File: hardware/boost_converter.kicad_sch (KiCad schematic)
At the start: 11 parts, among them SW1 SW_SPDT, U5 TPS61200DRC

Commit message: Removed comments on UART, added some footprints and started fixing rule checks
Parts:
- C10, C9: Manuf. Part # (none) -> GRM21BR71H104KA01L; Part Num GRM21BR71H104KA01L -> (none); Price/unit $0.0097 -> (none); Supplier Name (none) -> JLCPCB; Supplier Unit Price (none) -> $0.0097
- SW1: Supplier Name (none) -> JLCPCB
- U5: Manuf. Part # (none) -> TPS61200DRCR; Part Num TPS61200DRCR -> (none); Price/unit $1.4430 -> (none); Supplier Name (none) -> JLCPCB; Supplier Unit Price (none) -> $1.4430
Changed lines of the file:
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@@
+			)
+		)
+		(property "Supplier Name" ""
+			(at 193.04 106.68 0)
+			(effects
+				(font
+					(size 1.27 1.27)
+				)
+				(hide yes)
 			)
 		)
@@
 			)
 		)
+		(property "Supplier Name" ""
+			(at 118.11 111.76 0)
+			(effects
+				(font
+					(size 1.27 1.27)
+				)
+				(hide yes)
+			)
+		)
 		(pin "2"
 		)
@@
 			)
 		)
+		(property "Supplier Name" ""
+			(at 148.59 87.63 0)
+			(effects
+				(font
+					(size 1.27 1.27)
+				)
+				(hide yes)
+			)
+		)
 		(pin "1"
 		)
@@
 			)
 		)
-		(property "Part Num" "GRM21BR71H104KA01L"
-			(at 170.18 110.49 0)
-			(effects
-				(font
-					(size 1.27 1.27)
-				)
-				(hide yes)
-			)
-		)
-		(property "Price/unit" "$0.0097"
-			(at 170.18 110.49 0)
-			(effects
-				(font
-					(size 1.27 1.27)
-				)
-				(hide yes)
-			)
-		)
 		(property "Supplier Link" "https://jlcpcb.com/partdetail/MurataElectronics-GRM21BR71H104KA01L/C77082"
 			(at 170.18 110.49 0)
@@
 			)
 		)
+		(property "Supplier Name" "JLCPCB"
+			(at 170.18 110.49 0)
+			(effects
+				(font
+					(size 1.27 1.27)
+				)
+				(hide yes)
+			)
+		)
+		(property "Manuf. Part #" "GRM21BR71H104KA01L"
+			(at 170.18 110.49 0)
+			(effects
+				(font
+					(size 1.27 1.27)
+				)
+				(hide yes)
+			)
+		)
+		(property "Supplier Unit Price" "$0.0097"
+			(at 170.18 110.49 0)
+			(effects
+				(font
+					(size 1.27 1.27)
+				)
+				(hide yes)
+			)
+		)
 		(pin "1"
 		)
@@
 			)
 		)
+		(property "Supplier Name" ""
+			(at 110.49 105.41 0)
+			(effects
+				(font
+					(size 1.27 1.27)
+				)
+				(hide yes)
+			)
+		)
 		(pin "1"
 		)
@@
 		)
 		(property "Description" "Resistor, small symbol"
+			(at 184.15 111.76 0)
+			(effects
+				(font
+					(size 1.27 1.27)
+				)
+				(hide yes)
+			)
+		)
+		(property "Supplier Name" ""
 			(at 184.15 111.76 0)
 			(effects
@@
 			)
 		)
-		(property "Price/unit" ""
-			(at 44.45 149.86 0)
-			(effects
-				(font
-					(size 1.27 1.27)
-				)
-				(hide yes)
-			)
-		)
-		(property "Part Num" ""
-			(at 44.45 149.86 0)
-			(effects
-				(font
-					(size 1.27 1.27)
-				)
-				(hide yes)
-			)
-		)
 		(property "Package" ""
 			(at 44.45 149.86 0)
@@
 			)
 		)
+		(property "Supplier Name" "JLCPCB"
+			(at 44.45 149.86 0)
+			(effects
+				(font
+					(size 1.27 1.27)
+				)
+				(hide yes)
+			)
+		)
 		(pin "3"
 		)
@@
 			)
 		)
+		(property "Supplier Name" ""
+			(at 184.15 101.6 0)
+			(effects
+				(font
+					(size 1.27 1.27)
+				)
+				(hide yes)
+			)
+		)
 		(pin "2"
 		)
@@
 			)
 		)
-		(property "Part Num" "GRM21BR71H104KA01L"
-			(at 124.46 100.33 0)
-			(effects
-				(font
-					(size 1.27 1.27)
-				)
-				(hide yes)
-			)
-		)
-		(property "Price/unit" "$0.0097"
-			(at 124.46 100.33 0)
-			(effects
-				(font
-					(size 1.27 1.27)
-				)
-				(hide yes)
-			)
-		)
 		(property "Supplier Link" "https://jlcpcb.com/partdetail/MurataElectronics-GRM21BR71H104KA01L/C77082"
 			(at 124.46 100.33 0)
@@
 			)
 		)
+		(property "Supplier Name" "JLCPCB"
+			(at 124.46 100.33 0)
+			(effects
+				(font
+					(size 1.27 1.27)
+				)
+				(hide yes)
+			)
+		)
+		(property "Manuf. Part #" "GRM21BR71H104KA01L"
+			(at 124.46 100.33 0)
+			(effects
+				(font
+					(size 1.27 1.27)
+				)
+				(hide yes)
+			)
+		)
+		(property "Supplier Unit Price" "$0.0097"
+			(at 124.46 100.33 0)
+			(effects
+				(font
+					(size 1.27 1.27)
+				)
+				(hide yes)
+			)
+		)
 		(pin "1"
 		)
@@
 			)
 		)
+		(property "Supplier Name" ""
+			(at 118.11 100.33 0)
+			(effects
+				(font
+					(size 1.27 1.27)
+				)
+				(hide yes)
+			)
+		)
 		(pin "2"
 		)
@@
 			)
 		)
-		(property "Price/unit" "$1.4430"
-			(at 148.59 100.33 0)
-			(effects
-				(font
-					(size 1.27 1.27)
-				)
-				(hide yes)
-			)
-		)
-		(property "Part Num" "TPS61200DRCR"
-			(at 148.59 100.33 0)
-			(effects
-				(font
-					(size 1.27 1.27)
-				)
-				(hide yes)
-			)
-		)
 		(property "Package" "VSON-10-EP(3x3)"
 			(at 148.59 100.33 0)
 			(effects
+				(font
+					(size 1.27 1.27)
+				)
+				(hide yes)
+			)
+		)
+		(property "Supplier Name" "JLCPCB"
+			(at 148.59 100.33 0)
+			(effects
+				(font
+					(size 1.27 1.27)
+				)
+				(hide yes)
+			)
+		)
+		(property "Manuf. Part #" "TPS61200DRCR"
+			(at 148.59 100.33 0)
+			(effects
+				(font
+					(size 1.27 1.27)
+				)
+				(hide yes)
+			)
+		)
+		(property "Supplier Unit Price" "$1.4430"
+			(at 148.59 100.33 0)
+			(effects

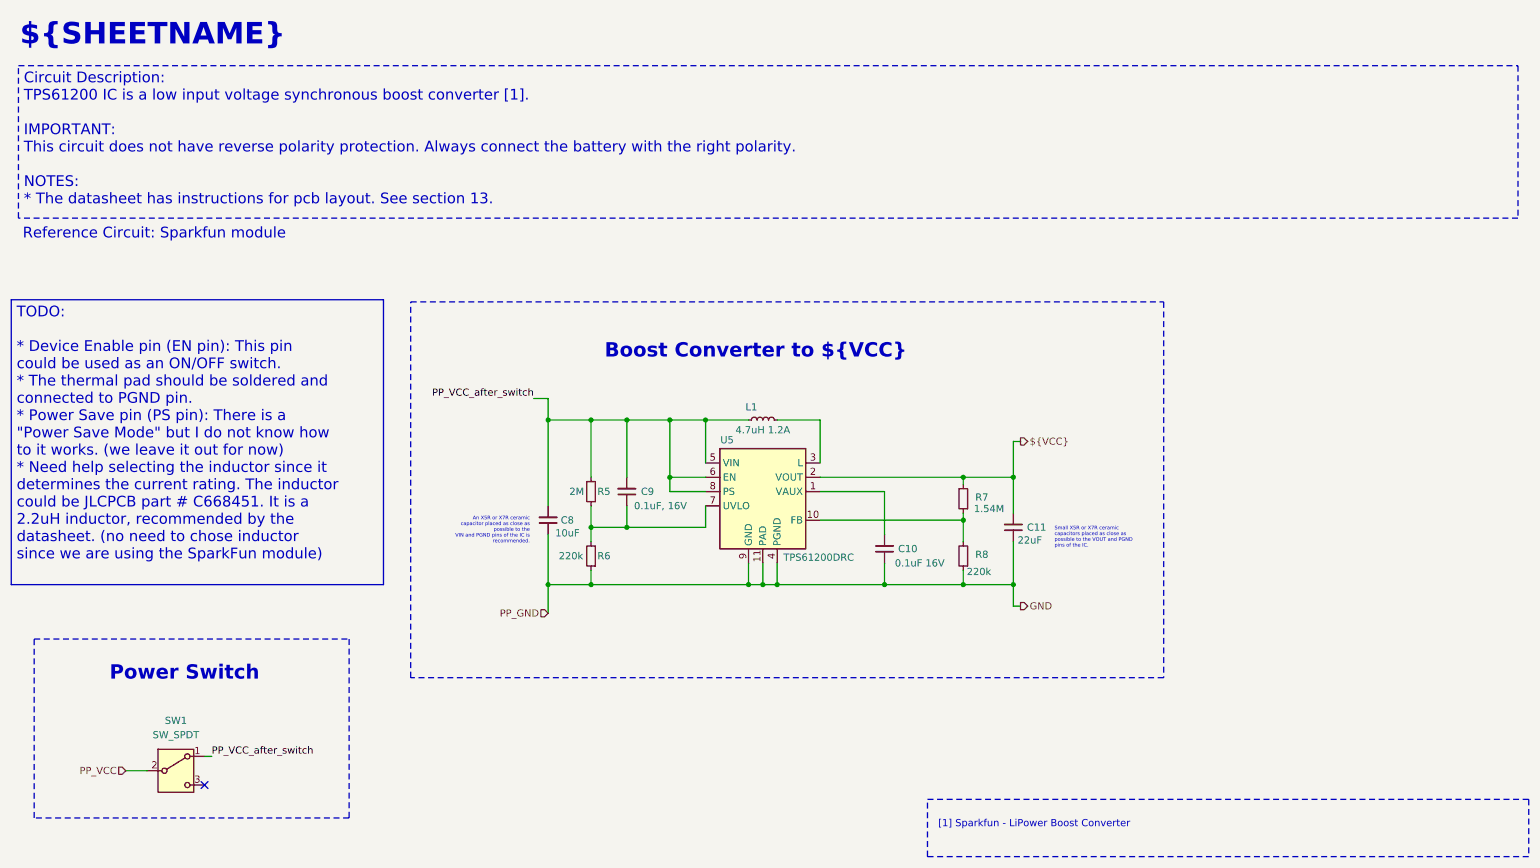
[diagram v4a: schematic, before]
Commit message: Added switch footprint, SparkFun_LiPower footprint
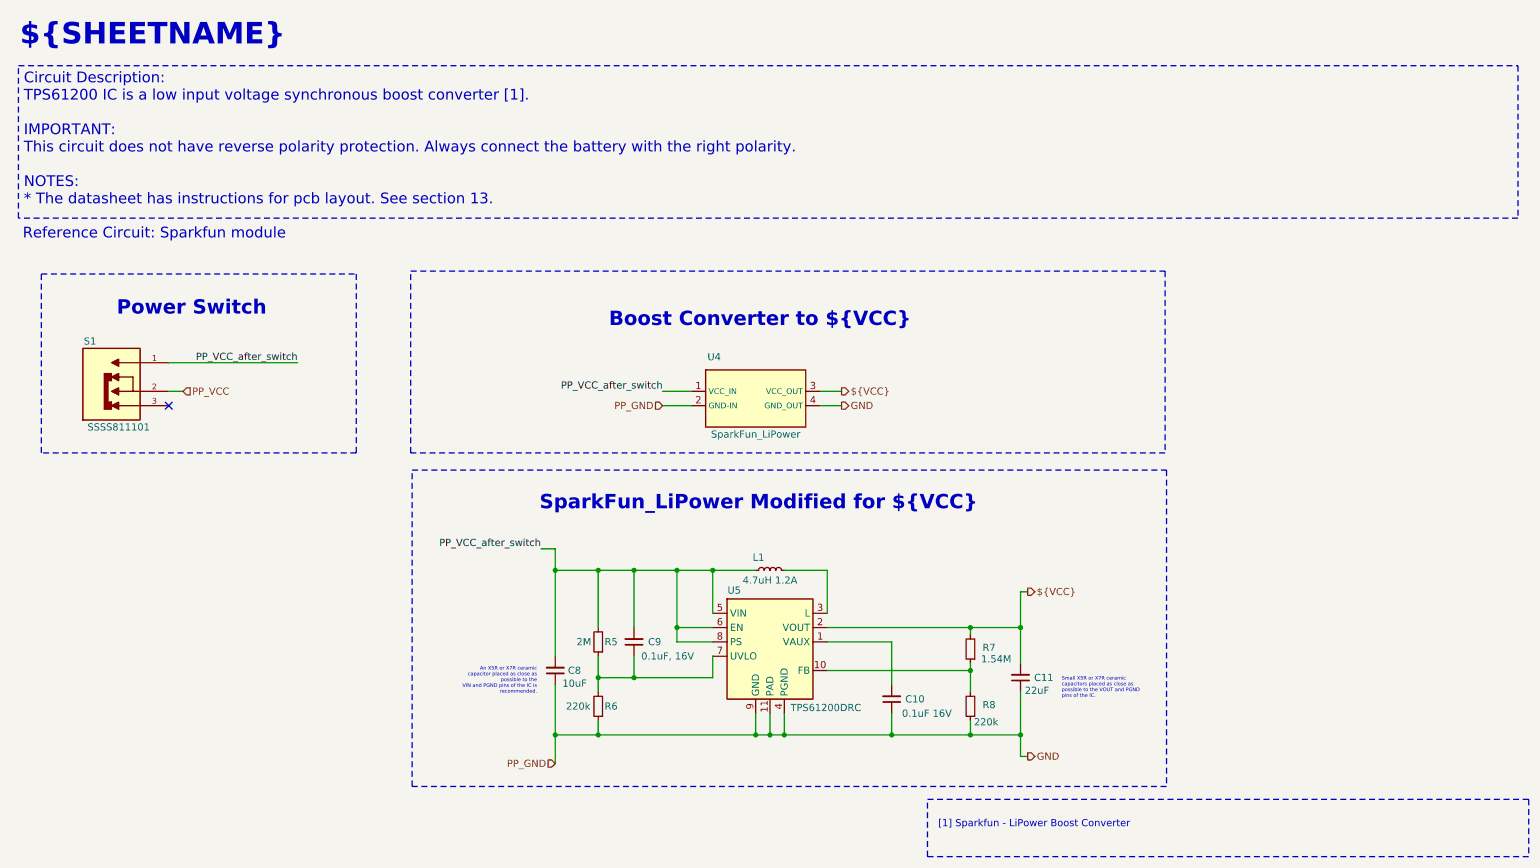
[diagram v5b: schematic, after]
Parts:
- removed SW1: SW_SPDT, symbol Switch:SW_SPDT
- added S1: SSSS811101, kitchen_timer:SW_SSSS811101, symbol kitchen_timer-symbols_lib:SSSS811101
- added U4: SparkFun_LiPower, kitchen_timer:SparkFun_LiPower, symbol kitchen_timer-symbols_lib:Sparkfun_LiPower-Boost_Converter
- C10, C11, C8, C9, L1, R5, R6, R7, R8, U5: now left out of the parts list
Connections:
- net ${VCC}: now also U4.3 (VCC_OUT)
- net GND: now also U4.2 (GND-IN), U4.4 (GND_OUT)
- net PP_VCC: now also S1.2
- net PP_VCC_after_switch: now also S1.1, U4.1 (VCC_IN)
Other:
- note added: "SparkFun_LiPower Modified for ${VCC}"
- moved on the sheet: C10, C11, C8, C9, L1, R5, R6, R7, R8, U5

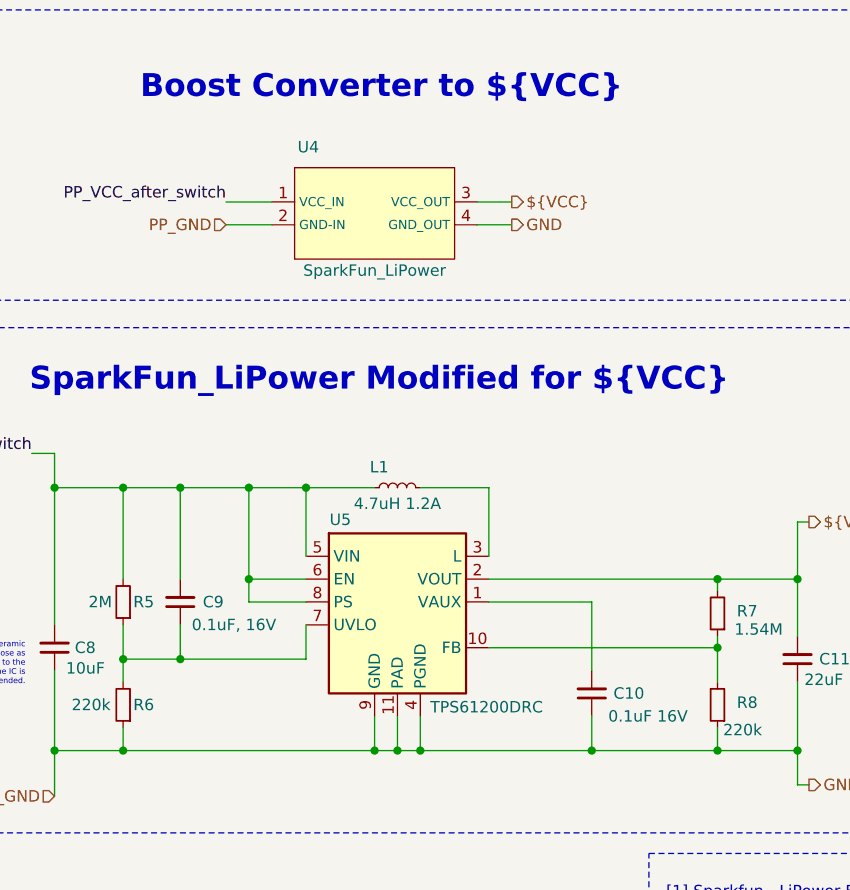
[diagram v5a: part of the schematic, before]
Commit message: Added many footprints and populated part of the property tables
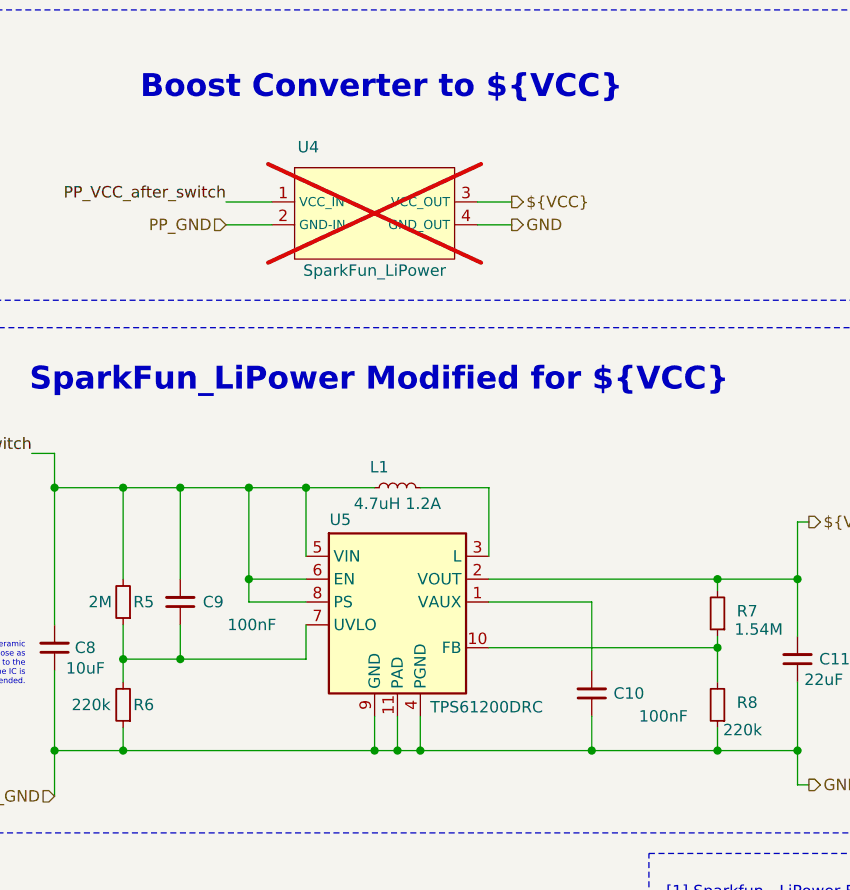
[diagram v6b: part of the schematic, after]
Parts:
- C10: value 0.1uF 16V -> 100nF; footprint (none) -> Capacitor_SMD:C_0805_2012Metric_Pad1.18x1.45mm_HandSolder; Manuf. Name (none) -> Murata Electronics; Supplier Link https://jlcpcb.com/partdetail/MurataElectronics-GRM21BR71H104KA01L/C77082 -> https://jlcpcb.com/partdetail/MurataElectronics-GRM21BR71H104KA01L/C77082; Supplier Part # (none) -> C77082; Supplier Unit Price $0.0097 -> $0.0099
- C11, C8: footprint (none) -> ~
- C9: value 0.1uF, 16V -> 100nF; footprint (none) -> Capacitor_SMD:C_0805_2012Metric_Pad1.18x1.45mm_HandSolder; Manuf. Name (none) -> Murata Electronics; Supplier Link https://jlcpcb.com/partdetail/MurataElectronics-GRM21BR71H104KA01L/C77082 -> https://jlcpcb.com/partdetail/MurataElectronics-GRM21BR71H104KA01L/C77082; Supplier Part # (none) -> C77082; Supplier Unit Price $0.0097 -> $0.0099
- U4: now not fitted; now left out of the parts list
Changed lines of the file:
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@@
 			)
 		)
-		(property "Footprint" ""
+		(property "Footprint" "~"
 			(at 194.31 133.35 0)
 			(effects
@@
 			)
 		)
-		(property "Description" "Unpolarized capacitor, small symbol"
+		(property "Description" "22uF Unpolarized capacitor"
 			(at 194.31 133.35 0)
 			(effects
@@
 			)
 		)
-		(property "Supplier Name" ""
+		(property "Supplier Name" "~"
+			(at 194.31 133.35 0)
+			(effects
+				(font
+					(size 1.27 1.27)
+				)
+				(hide yes)
+			)
+		)
+		(property "Manuf. Name" "~"
+			(at 194.31 133.35 0)
+			(effects
+				(font
+					(size 1.27 1.27)
+				)
+				(hide yes)
+			)
+		)
+		(property "Manuf. Part #" "~"
+			(at 194.31 133.35 0)
+			(effects
+				(font
+					(size 1.27 1.27)
+				)
+				(hide yes)
+			)
+		)
+		(property "Package" "~"
+			(at 194.31 133.35 0)
+			(effects
+				(font
+					(size 1.27 1.27)
+				)
+				(hide yes)
+			)
+		)
+		(property "Supplier Link" "~"
+			(at 194.31 133.35 0)
+			(effects
+				(font
+					(size 1.27 1.27)
+				)
+				(hide yes)
+			)
+		)
+		(property "Supplier Part #" "~"
+			(at 194.31 133.35 0)
+			(effects
+				(font
+					(size 1.27 1.27)
+				)
+				(hide yes)
+			)
+		)
+		(property "Supplier Unit Price" "~"
 			(at 194.31 133.35 0)
 			(effects
@@
 			)
 		)
-		(property "Supplier Name" ""
+		(property "Supplier Name" "~"
 			(at 149.86 114.3 0)
 			(effects
@@
 				)
 				(hide yes)
+			)
+		)
+		(property "Manuf. Name" "~"
+			(at 149.86 114.3 0)
+			(effects
+				(font
+					(size 1.27 1.27)
+				)
+			)
+		)
+		(property "Manuf. Part #" "~"
+			(at 149.86 114.3 0)
+			(effects
+				(font
+					(size 1.27 1.27)
+				)
+			)
+		)
+		(property "Package" "~"
+			(at 149.86 114.3 0)
+			(effects
+				(font
+					(size 1.27 1.27)
+				)
+			)
+		)
+		(property "Supplier Link" "~"
+			(at 149.86 114.3 0)
+			(effects
+				(font
+					(size 1.27 1.27)
+				)
+			)
+		)
+		(property "Supplier Part #" "~"
+			(at 149.86 114.3 0)
+			(effects
+				(font
+					(size 1.27 1.27)
+				)
+			)
+		)
+		(property "Supplier Unit Price" "~"
+			(at 149.86 114.3 0)
+			(effects
+				(font
+					(size 1.27 1.27)
+				)
 			)
 		)
@@
 			)
 		)
-		(property "Value" "0.1uF 16V"
+		(property "Value" "100nF"
 			(at 182.118 139.7 0)
 			(effects
@@
 			)
 		)
-		(property "Footprint" ""
+		(property "Footprint" "Capacitor_SMD:C_0805_2012Metric_Pad1.18x1.45mm_HandSolder"
 			(at 171.45 137.16 0)
 			(effects
@@
 			)
 		)
-		(property "Description" "Unpolarized capacitor, small symbol"
+		(property "Description" "100nF Unpolarized capacitor"
 			(at 171.45 137.16 0)
 			(effects
@@
 			)
 		)
-		(property "Supplier Link" "https://jlcpcb.com/partdetail/MurataElectronics-GRM21BR71H104KA01L/C77082"
+		(property "Supplier Link" "https://jlcpcb.com/partdetail/MurataElectronics-GRM21BR71H104KA01L/C77082 "
 			(at 171.45 137.16 0)
 			(effects
@@
 			)
 		)
-		(property "Supplier Unit Price" "$0.0097"
+		(property "Supplier Unit Price" " $0.0099"
+			(at 171.45 137.16 0)
+			(effects
+				(font
+					(size 1.27 1.27)
+				)
+				(hide yes)
+			)
+		)
+		(property "Manuf. Name" " Murata Electronics"
+			(at 171.45 137.16 0)
+			(effects
+				(font
+					(size 1.27 1.27)
+				)
+				(hide yes)
+			)
+		)
+		(property "Supplier Part #" "C77082"
 			(at 171.45 137.16 0)
 			(effects
@@
 			)
 		)
-		(property "Footprint" ""
+		(property "Footprint" "~"
 			(at 111.76 132.08 0)
 			(effects
@@
 			)
 		)
-		(property "Description" "Unpolarized capacitor, small symbol"
+		(property "Description" "10uF Unpolarized capacitor"
 			(at 111.76 132.08 0)
 			(effects
@@
 			)
 		)
-		(property "Supplier Name" ""
+		(property "Supplier Name" "~"
+			(at 111.76 132.08 0)
+			(effects
+				(font
+					(size 1.27 1.27)
+				)
+				(hide yes)
+			)
+		)
+		(property "Manuf. Name" "~"
+			(at 111.76 132.08 0)
+			(effects
+				(font
+					(size 1.27 1.27)
+				)
+				(hide yes)
+			)
+		)
+		(property "Manuf. Part #" "~"
+			(at 111.76 132.08 0)
+			(effects
+				(font
+					(size 1.27 1.27)
+				)
+				(hide yes)
+			)
+		)
+		(property "Package" "~"
+			(at 111.76 132.08 0)
+			(effects
+				(font
+					(size 1.27 1.27)
+				)
+				(hide yes)
+			)
+		)
+		(property "Supplier Link" "~"
+			(at 111.76 132.08 0)
+			(effects
+				(font
+					(size 1.27 1.27)
+				)
+				(hide yes)
+			)
+		)
+		(property "Supplier Part #" "~"
+			(at 111.76 132.08 0)
+			(effects
+				(font
+					(size 1.27 1.27)
+				)
+				(hide yes)
+			)
+		)
+		(property "Supplier Unit Price" "~"
 			(at 111.76 132.08 0)
 			(effects
@@
 			)
 		)
-		(property "Value" "0.1uF, 16V"
+		(property "Value" "100nF"
 			(at 136.398 129.54 0)
 			(effects
@@
 			)
 		)
-		(property "Footprint" ""
+		(property "Footprint" "Capacitor_SMD:C_0805_2012Metric_Pad1.18x1.45mm_HandSolder"
 			(at 125.73 127 0)
 			(effects
@@
 			)
 		)
-		(property "Description" "Unpolarized capacitor, small symbol"
+		(property "Description" "100nF Unpolarized capacitor"
 			(at 125.73 127 0)
 			(effects
@@
 			)
 		)
-		(property "Supplier Link" "https://jlcpcb.com/partdetail/MurataElectronics-GRM21BR71H104KA01L/C77082"
+		(property "Supplier Link" "https://jlcpcb.com/partdetail/MurataElectronics-GRM21BR71H104KA01L/C77082 "
 			(at 125.73 127 0)
 			(effects
@@
 			)
 		)
-		(property "Supplier Unit Price" "$0.0097"
+		(property "Supplier Unit Price" " $0.0099"
+			(at 125.73 127 0)
+			(effects
+				(font
+					(size 1.27 1.27)
+				)
+				(hide yes)
+			)
+		)
+		(property "Manuf. Name" " Murata Electronics"
+			(at 125.73 127 0)
+			(effects
+				(font
+					(size 1.27 1.27)
+				)
+				(hide yes)
+			)
+		)
+		(property "Supplier Part #" "C77082"
 			(at 125.73 127 0)
 			(effects
@@
 		(unit 1)
 		(exclude_from_sim no)
-		(in_bom yes)
+		(in_bom no)
 		(on_board yes)
-		(dnp no)
+		(dnp yes)
 		(property "Reference" "U4"
 			(at 139.954 76.454 0)
